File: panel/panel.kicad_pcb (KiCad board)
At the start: 4 copper layers, 36 x 36 mm, 288 parts, among them J1 IN, J2 OUT, Q1 Q_PMOS_GSD, Q10 Q_PMOS_GSD, Q11 Q_PMOS_GSD, Q12 Q_PMOS_GSD, Q13 Q_PMOS_GSD, Q14 Q_PMOS_GSD, Q15 Q_PMOS_GSD, Q16 Q_PMOS_GSD, Q2 Q_PMOS_GSD, Q3 Q_PMOS_GSD, Q4 Q_PMOS_GSD, Q5 Q_PMOS_GSD, Q6 Q_PMOS_GSD, Q7 Q_PMOS_GSD, Q8 Q_PMOS_GSD, Q9 Q_PMOS_GSD, U1 TLC59025, U2 TLC59025, U3 TLC59025, U4 SN74HC595, U5 SN74HC595, U6 NC7WZ17, U7 NC7WZ17

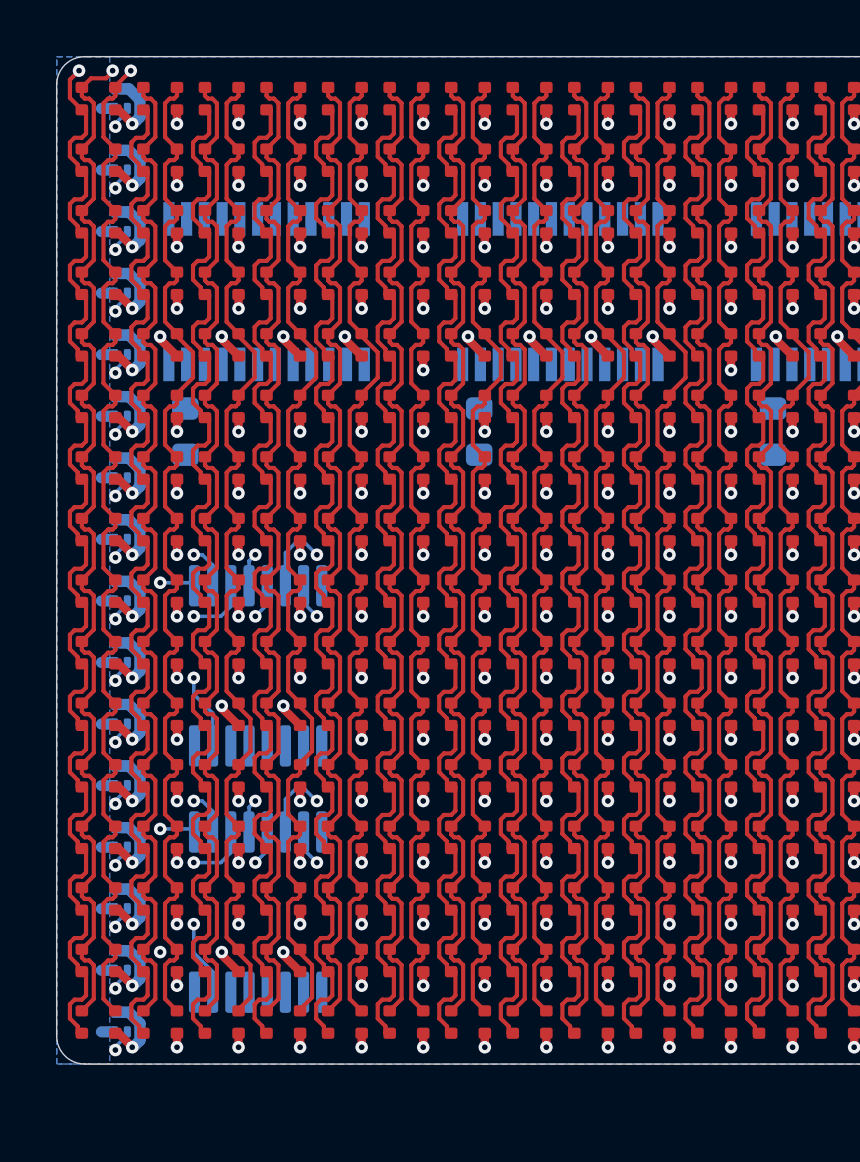
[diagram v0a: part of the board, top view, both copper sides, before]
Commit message: Routed first 8 columns of blue and green channels
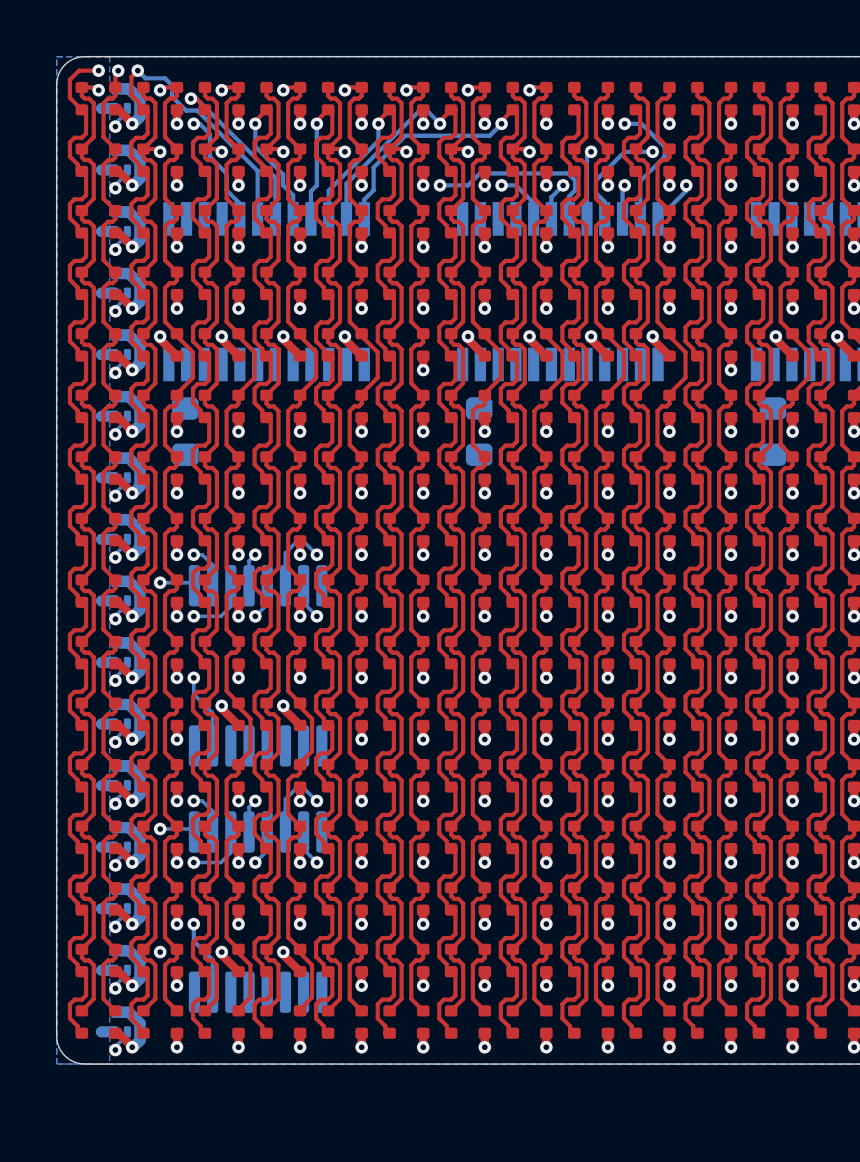
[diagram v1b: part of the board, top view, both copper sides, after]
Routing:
- net COL_0G: track 41.1 -> 58.9 mm, vias 1 -> 2
- net COL_4G: track 39.7 -> 57.1 mm, vias 0 -> 2
- net COL_1G: track 39.7 -> 56.6 mm, vias 0 -> 2
- net COL_2G: track 39.7 -> 55.2 mm, vias 0 -> 2
- net COL_3G: track 39.7 -> 54.2 mm, vias 0 -> 2
- net COL_6G: track 39.7 -> 51.7 mm, vias 0 -> 2
- net COL_5G: track 39.7 -> 49.9 mm, vias 0 -> 2
- net COL_1B: track 45.1 -> 54.6 mm, vias 0 -> 1
- net COL_0B: track 46.8 -> 56.2 mm, vias 1 -> 2
- net COL_7G: track 39.7 -> 48.1 mm, vias 0 -> 2
- net COL_7B: track 45.1 -> 53.0 mm, vias 0 -> 1
- net COL_6B: track 45.1 -> 51.6 mm, vias 0 -> 1
- net COL_2B: track 45.1 -> 51.6 mm, vias 0 -> 1
- net /ROW_8: track 24.8 -> 19.0 mm
- net COL_5B: track 45.1 -> 49.9 mm, vias 0 -> 1
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
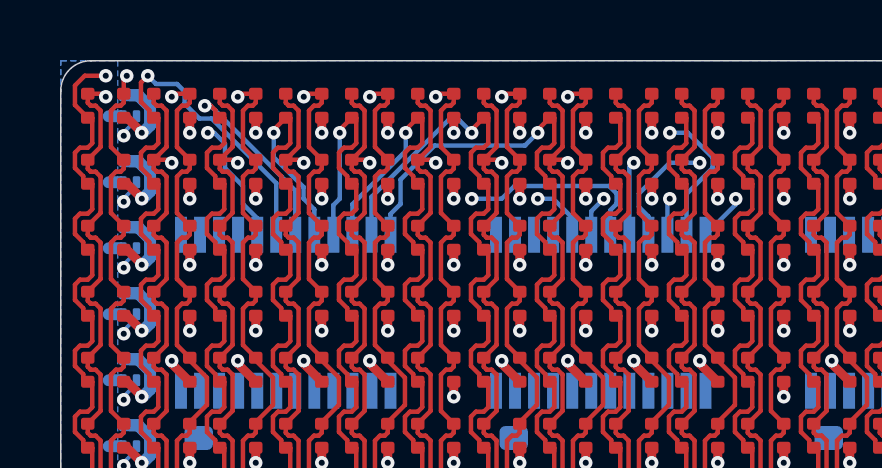
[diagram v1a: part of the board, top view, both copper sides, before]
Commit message: Modified copper pours
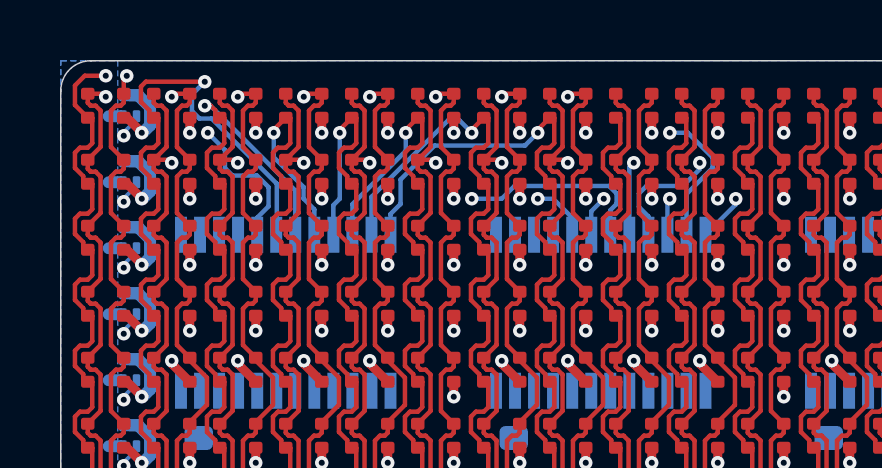
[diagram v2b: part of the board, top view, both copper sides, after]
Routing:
- net COL_1B: track 54.6 -> 55.3 mm
- net COL_0B: track 56.2 -> 56.9 mm

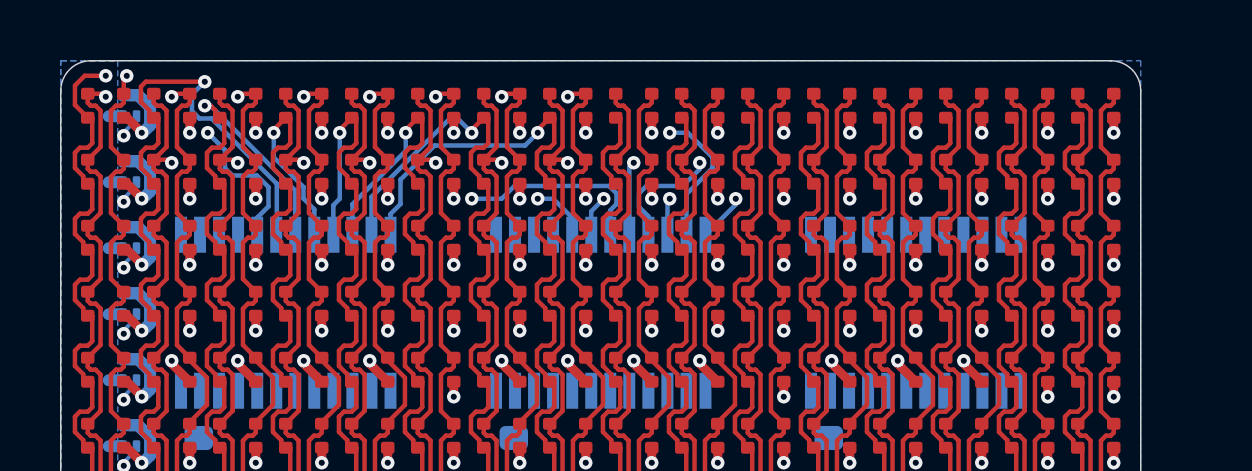
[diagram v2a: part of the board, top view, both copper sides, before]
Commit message: Columns 0-7 of R/G/B channels fully routed
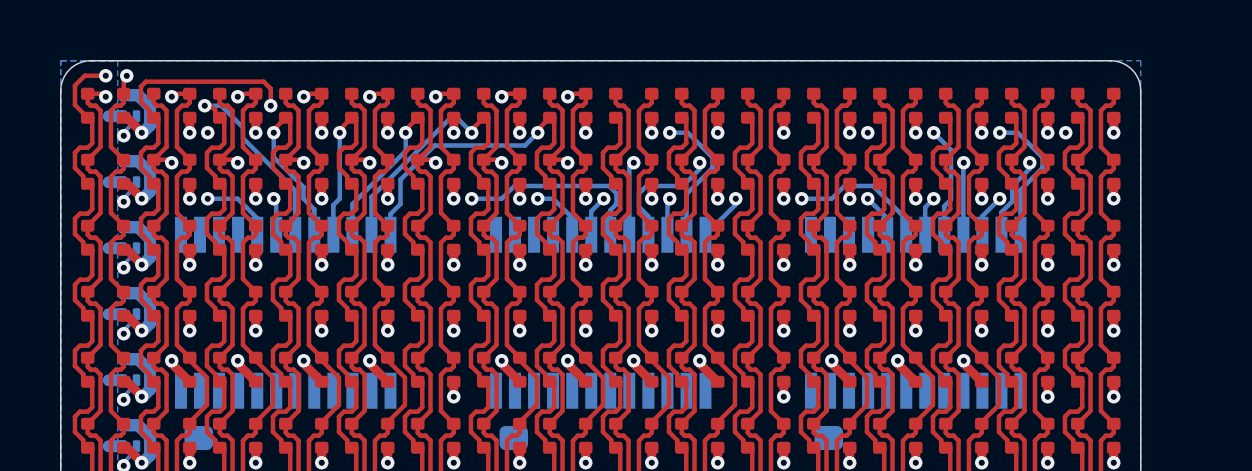
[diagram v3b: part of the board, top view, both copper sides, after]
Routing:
- net COL_0R: track 40.5 -> 83.9 mm, vias 1 -> 2
- net COL_1R: track 40.4 -> 72.5 mm, vias 1 -> 3
- net COL_5R: track 40.4 -> 67.2 mm, vias 1 -> 3
- net COL_2R: track 40.2 -> 66.6 mm, vias 1 -> 2
- net COL_3R: track 40.2 -> 65.4 mm, vias 1 -> 2
- net COL_6R: track 40.4 -> 65.5 mm, vias 1 -> 2
- net COL_4R: track 40.4 -> 63.9 mm, vias 1 -> 2
- net COL_7R: track 40.4 -> 59.9 mm, vias 1 -> 2
- net COL_1B: track 55.3 -> 57.6 mm, vias 1 -> 2
- net COL_0B: track 56.9 -> 56.6 mm, vias 2 -> 3

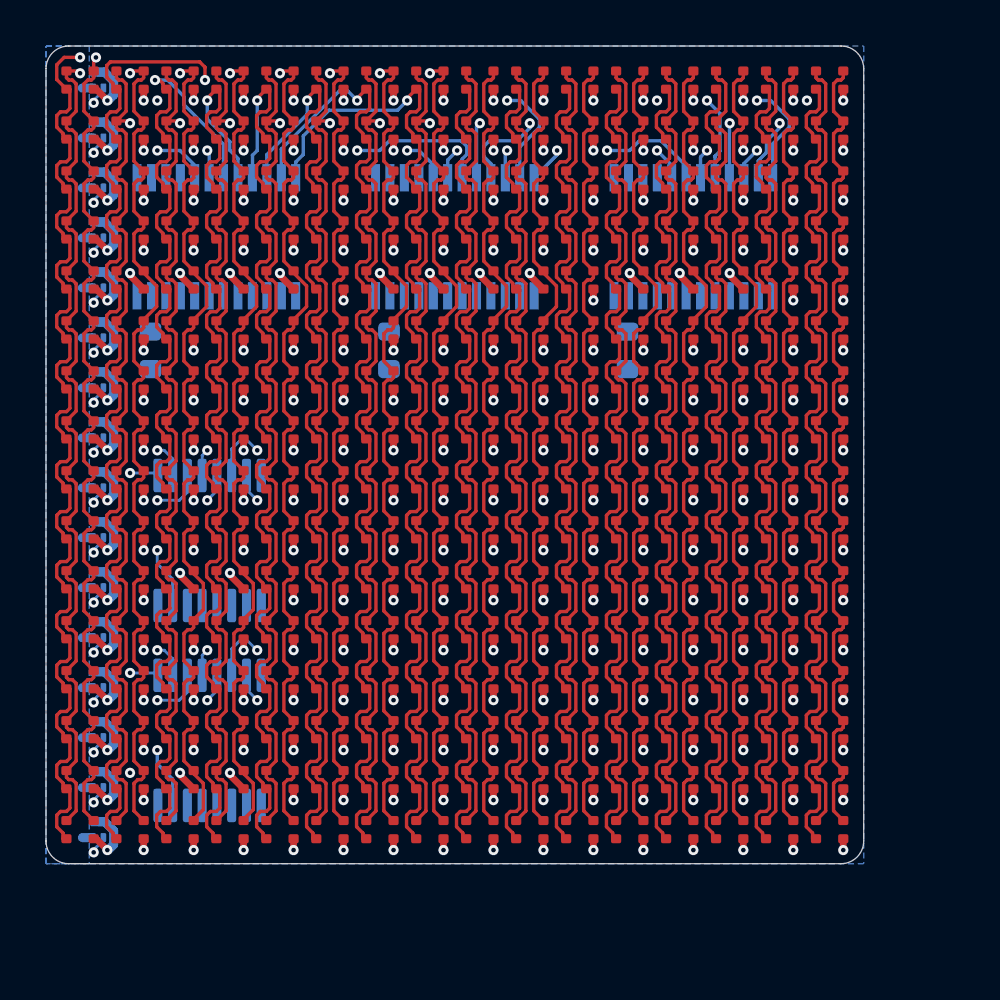
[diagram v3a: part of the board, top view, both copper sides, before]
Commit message: Routed columns 7-15 of blue channel
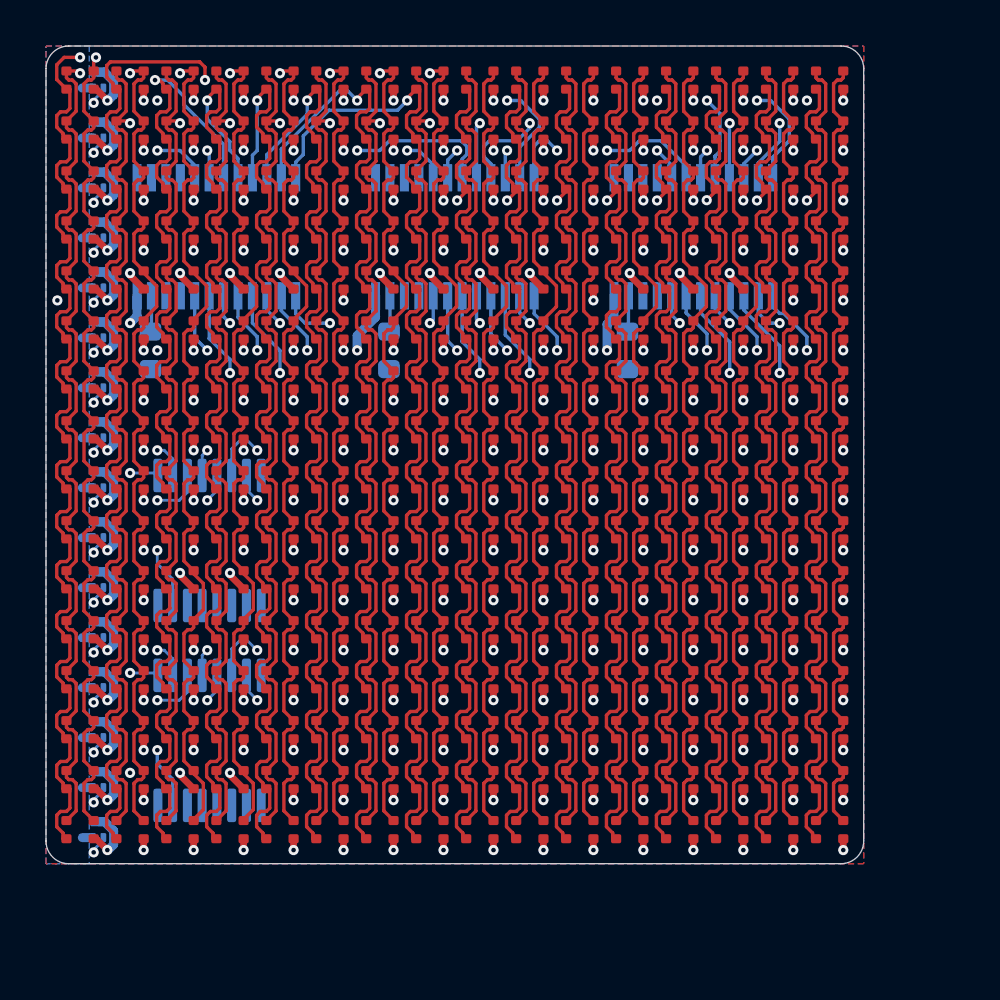
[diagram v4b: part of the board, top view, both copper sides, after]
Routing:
- net COL_15B: track 45.1 -> 81.9 mm, vias 0 -> 2
- net COL_14B: track 45.1 -> 78.9 mm, vias 0 -> 2
- net VCC: track 6.40 -> 38.8 mm, vias 0 -> 4
- net COL_13B: track 45.1 -> 75.5 mm, vias 0 -> 2
- net COL_12B: track 45.1 -> 72.6 mm, vias 0 -> 2
- net COL_11B: track 45.1 -> 69.4 mm, vias 0 -> 2
- net COL_10B: track 45.1 -> 64.8 mm, vias 0 -> 2
- net COL_9B: track 45.1 -> 61.7 mm, vias 0 -> 2
- net COL_8B: track 45.1 -> 57.4 mm, vias 0 -> 2
- net /ROW_3: track 16.6 -> 21.7 mm, vias 2 -> 3
- net COL_10R: track 39.7 -> 43.8 mm, vias 0 -> 1
- net COL_13R: track 39.7 -> 43.7 mm, vias 0 -> 1
- net COL_10G: track 39.7 -> 43.6 mm, vias 0 -> 1
- net COL_13G: track 39.7 -> 43.4 mm, vias 0 -> 1
- net COL_8R: track 39.7 -> 42.9 mm, vias 0 -> 1
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- added copper zone on F.Cu, net GND
- added copper zone on In2.Cu, net GND
